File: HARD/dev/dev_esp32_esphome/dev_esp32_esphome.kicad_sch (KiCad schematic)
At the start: 67 parts, among them J1 USB4105-GF-A, Q1 DMG3415U, SW1 SW_Push, SW2 SW_Push, U1 SHTC3, U2 ICM-42670-P, U3 ESP32-C3-MINI-1, U4 MCP73831T-2ACI/OT, U5 Rust_Board, U6 SY8088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

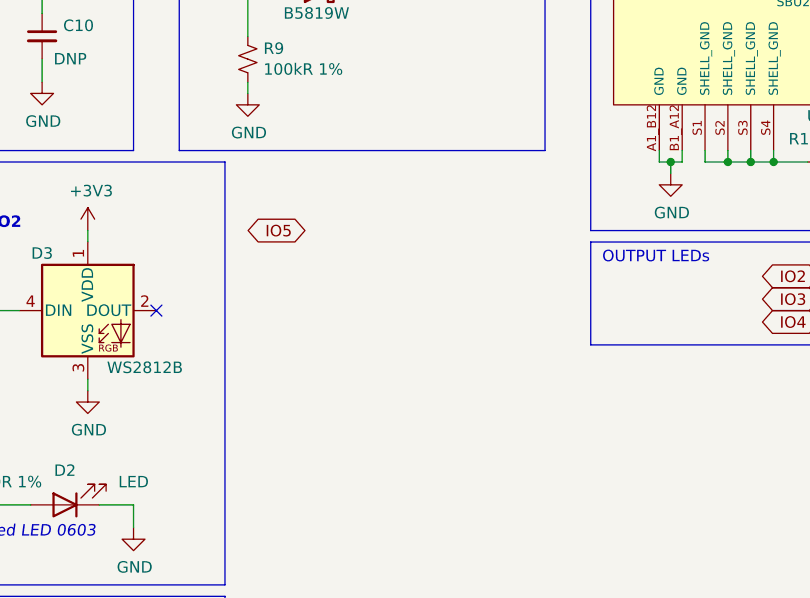
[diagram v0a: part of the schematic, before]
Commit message: Colocation of componentes, no enroute
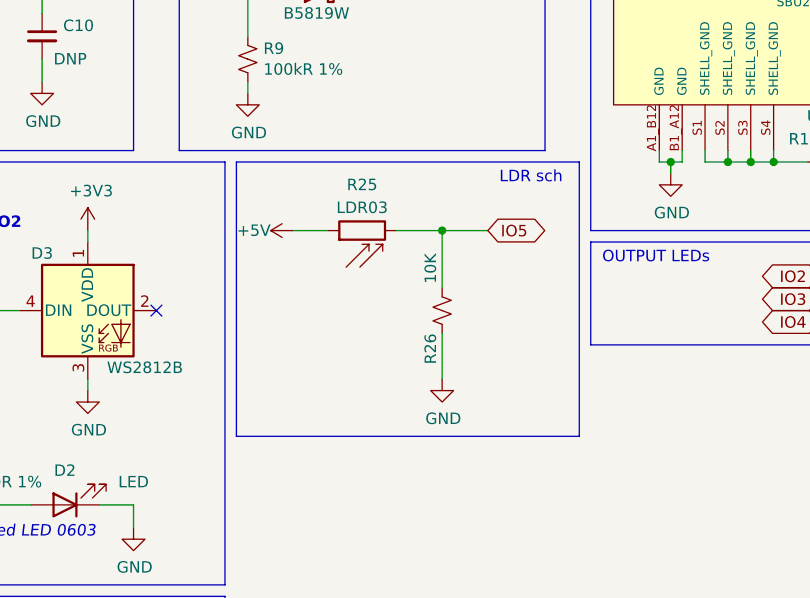
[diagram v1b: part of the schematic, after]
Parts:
- added R25: LDR03, OptoDevice:R_LDR_10x8.5mm_P7.6mm_Vertical, symbol Sensor_Optical:LDR03
- added R26: 10K, Resistor_SMD:R_0402_1005Metric, symbol Device:R_Small_US
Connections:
- net +5V: now also R25.1
- net GND: now also R26.1
- net IO5: now also R25.2, R26.2
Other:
- note added: "LDR sch"
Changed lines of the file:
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@@
   (junction (at 313.69 99.06) (diameter 0) (color 0 0 0 0)
   )
+  (junction (at 185.42 109.22) (diameter 0) (color 0 0 0 0)
+  )
   (junction (at 163.83 76.2) (diameter 0) (color 0 0 0 0)
   )
@@
     (stroke (width 0) (type default))
   )
+  (wire (pts (xy 180.34 109.22) (xy 185.42 109.22))
+    (stroke (width 0) (type default))
+  )
   (wire (pts (xy 81.28 158.75) (xy 81.28 156.21))
     (stroke (width 0) (type default))
@@
     (stroke (width 0) (type default))
   )
+  (wire (pts (xy 185.42 109.22) (xy 185.42 115.57))
+    (stroke (width 0) (type default))
+  )
   (wire (pts (xy 369.57 54.61) (xy 369.57 60.96))
     (stroke (width 0) (type default))
@@
     (stroke (width 0) (type default))
   )
+  (wire (pts (xy 185.42 109.22) (xy 190.5 109.22))
+    (stroke (width 0) (type default))
+  )
   (wire (pts (xy 246.38 22.86) (xy 262.89 22.86))
     (stroke (width 0) (type default))
@@
     (stroke (width 0) (type default))
   )
+  (wire (pts (xy 185.42 120.65) (xy 185.42 125.73))
+    (stroke (width 0) (type default))
+  )
   (wire (pts (xy 233.68 74.93) (xy 233.68 76.2))
     (stroke (width 0) (type default))
@@
     (stroke (width 0) (type default))
   )
+  (wire (pts (xy 168.91 109.22) (xy 172.72 109.22))
+    (stroke (width 0) (type default))
+  )
   (polyline (pts (xy 115.57 101.6) (xy 161.29 101.6))
     (stroke (width 0) (type default))
@@
     (fill (type none))
   )
+  (rectangle (start 162.56 101.6) (end 200.66 132.08)
+    (stroke (width 0) (type default))
+    (fill (type none))
+  )
   (text "Board Connectors/Pin layout" (at 288.29 15.24 0)
     (effects (font (size 1.27 1.27) (thickness 0.254) bold) (justify left bottom))
@@
     (effects (font (size 1.27 1.27) italic) (justify left bottom))
   )
+  (text "LDR sch" (at 191.77 104.14 0)
+    (effects (font (size 1.27 1.27)) (justify left bottom))
+  )
   (text "Buttons (Reset & Boot)" (at 116.84 152.4 0)
     (effects (font (size 1.27 1.27) (thickness 0.254) bold) (justify left bottom))
@@
     )
   )
+  (global_label "IO5" (shape bidirectional) (at 190.5 109.22 0) (fields_autoplaced)
+    (effects (font (size 1.27 1.27)) (justify left))
+    (property "Intersheetrefs" "${INTERSHEET_REFS}" (at 197.6619 109.22 0)
+      (effects (font (size 1.27 1.27)) (justify left) hide)
+    )
+  )
   (global_label "USB_D-" (shape bidirectional) (at 254 76.2 0) (fields_autoplaced)
     (effects (font (size 1.27 1.27)) (justify left))
@@
     )
   )
-  (global_label "IO5" (shape bidirectional) (at 170.18 109.22 180) (fields_autoplaced)
-    (effects (font (size 1.27 1.27)) (justify right))
-    (property "Intersheetrefs" "${INTERSHEET_REFS}" (at 163.0181 109.22 0)
-      (effects (font (size 1.27 1.27)) (justify right) hide)
-    )
-  )
   (global_label "ENABLE" (shape input) (at 350.52 38.1 0) (fields_autoplaced)
     (effects (font (size 1.27 1.27)) (justify left))
@@
     )
   )
+  (symbol (lib_id "power:+5V") (at 168.91 109.22 90) (unit 1)
+    (in_bom yes) (on_board yes) (dnp no)
+    (property "Reference" "#PWR067" (at 172.72 109.22 0)
+      (effects (font (size 1.27 1.27)) hide)
+    )
+    (property "Value" "+5V" (at 166.37 109.22 90)
+      (effects (font (size 1.27 1.27)) (justify left))
+    )
+    (property "Footprint" "" (at 168.91 109.22 0)
+      (effects (font (size 1.27 1.27)) hide)
+    )
+    (property "Datasheet" "" (at 168.91 109.22 0)
+      (effects (font (size 1.27 1.27)) hide)
+    )
+    (pin "1")
+    (instances
+      (project "dev_esp32_esphome"
+        (path "/022bcc26-2461-4ab6-b205-d7326b84ebe5"
+          (reference "#PWR067") (unit 1)
+        )
+      )
+      (project "esp-rust-board"
+        (path "/196a8dd5-5fd6-4c7f-ae4a-0104bd82e61b"
+          (reference "#PWR0157") (unit 1)
+        )
+      )
+    )
+  )
   (symbol (lib_id "PCM_Espressif:ESP32-C3-MINI-1") (at 66.04 69.85 0) (unit 1)
     (in_bom yes) (on_board yes) (dnp no) (fields_autoplaced)
@@
     )
   )
+  (symbol (lib_id "Sensor_Optical:LDR03") (at 176.53 109.22 90) (unit 1)
+    (in_bom yes) (on_board yes) (dnp no) (fields_autoplaced)
+    (property "Reference" "R25" (at 176.53 104.14 90)
+      (effects (font (size 1.27 1.27)))
+    )
+    (property "Value" "LDR03" (at 176.53 106.68 90)
+      (effects (font (size 1.27 1.27)))
+    )
+    (property "Footprint" "OptoDevice:R_LDR_10x8.5mm_P7.6mm_Vertical" (at 176.53 104.775 90)
+      (effects (font (size 1.27 1.27)) hide)
+    )
+    (property "Datasheet" "http://www.elektronica-componenten.nl/WebRoot/StoreNL/Shops/61422969/54F1/BA0C/C664/31B9/2173/C0A8/2AB9/2AEF/LDR03IMP.pdf" (at 177.8 109.22 0)
+      (effects (font (size 1.27 1.27)) hide)
+    )
+    (pin "1")
+    (pin "2")
+    (instances
+      (project "dev_esp32_esphome"
+        (path "/022bcc26-2461-4ab6-b205-d7326b84ebe5"
+          (reference "R25") (unit 1)
+        )
+      )
+    )
+  )
   (symbol (lib_id "Device:R_Small_US") (at 228.6 101.6 90) (unit 1)
     (in_bom yes) (on_board yes) (dnp no)
@@
     )
   )
+  (symbol (lib_id "Device:R_Small_US") (at 185.42 118.11 180) (unit 1)
+    (in_bom yes) (on_board yes) (dnp no)
+    (property "Reference" "R26" (at 184.15 120.65 90)
+      (effects (font (size 1.27 1.27)) (justify left))
+    )
+    (property "Value" "10K" (at 184.15 111.76 90)
+      (effects (font (size 1.27 1.27)) (justify left))
+    )
+    (property "Footprint" "Resistor_SMD:R_0402_1005Metric" (at 185.42 118.11 0)
+      (effects (font (size 1.27 1.27)) hide)
+    )
+    (property "Datasheet" "~" (at 185.42 118.11 0)
+      (effects (font (size 1.27 1.27)) hide)
+    )
+    (property "LCSC" "C25117" (at 185.42 118.11 0)
+      (effects (font (size 1.27 1.27)) hide)
+    )
+    (pin "1")
+    (pin "2")
+    (instances
+      (project "dev_esp32_esphome"
+        (path "/022bcc26-2461-4ab6-b205-d7326b84ebe5"
+          (reference "R26") (unit 1)
+        )
+      )
+      (project "esp-rust-board"
+        (path "/196a8dd5-5fd6-4c7f-ae4a-0104bd82e61b"
+          (reference "R10") (unit 1)
+        )
+      )
+    )
+  )
   (symbol (lib_id "power:GND") (at 142.24 48.26 0) (unit 1)
     (in_bom yes) (on_board yes) (dnp no)
@@
         )
       )
+    )
+  )
+  (symbol (lib_id "power:GND") (at 185.42 125.73 0) (unit 1)
+    (in_bom yes) (on_board yes) (dnp no)
+    (property "Reference" "#PWR068" (at 185.42 132.08 0)
+      (effects (font (size 1.27 1.27)) hide)
+    )
+    (property "Value" "GND" (at 185.547 130.1242 0)
+      (effects (font (size 1.27 1.27)))
+    )
+    (property "Footprint" "" (at 185.42 125.73 0)
+      (effects (font (size 1.27 1.27)) hide)
+    )
+    (property "Datasheet" "" (at 185.42 125.73 0)
+      (effects (font (size 1.27 1.27)) hide)
+    )
+    (pin "1")
+    (instances
+      (project "dev_esp32_esphome"
+        (path "/022bcc26-2461-4ab6-b205-d7326b84ebe5"
+          (reference "#PWR068") (unit 1)
+        )
+      )
+      (project "esp-rust-board"
+        (path "/196a8dd5-5fd6-4c7f-ae4a-0104bd82e61b"
+          (reference "#PWR0136") (unit 1)
+        )
+      )
